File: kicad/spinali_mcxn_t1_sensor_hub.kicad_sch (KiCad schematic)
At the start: 0 parts

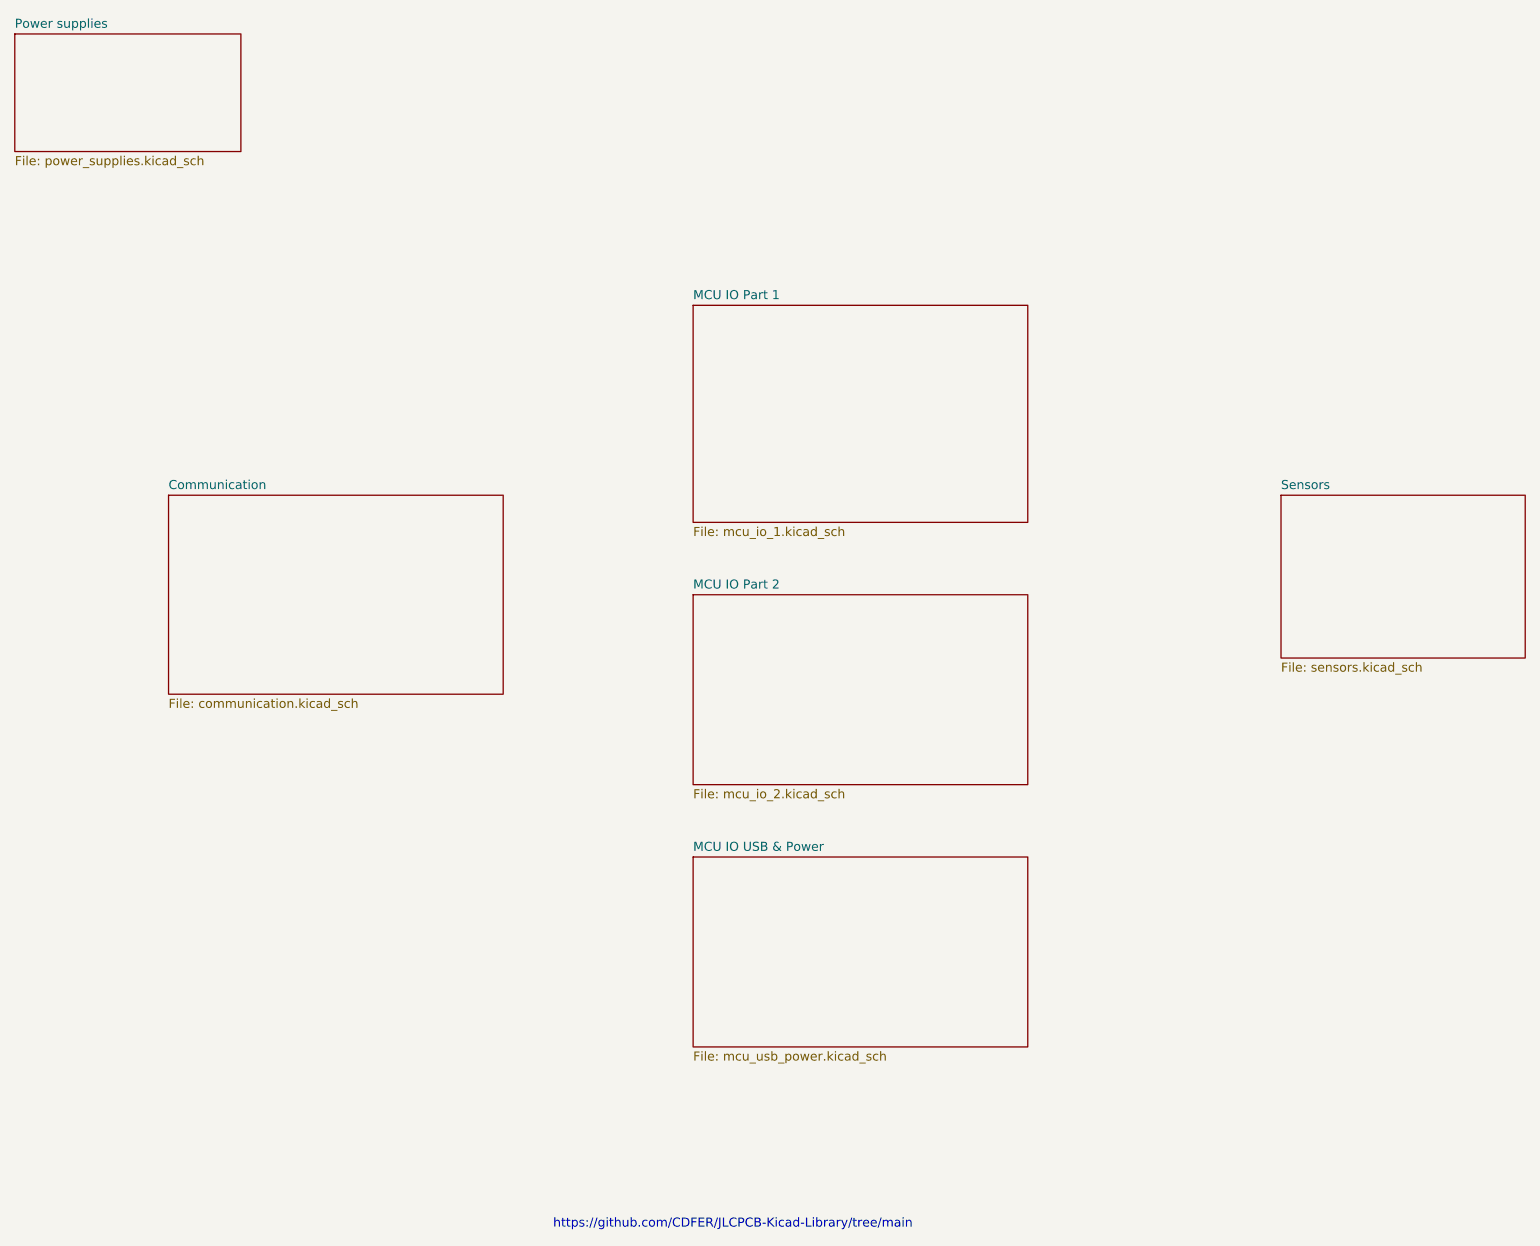
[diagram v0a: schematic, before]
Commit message: Updated schematics and BOM.
- Finished power supply schematics
- Added power schematic around MCXN
- Assigned MCXN pins
- Created board-to-board schematic and assigned pins to DF40T board-to-board connector
- Added correct sensors, finished sensor schematic
- Updated parts in communication schematic
- Added all part numbers etc in parts parameters
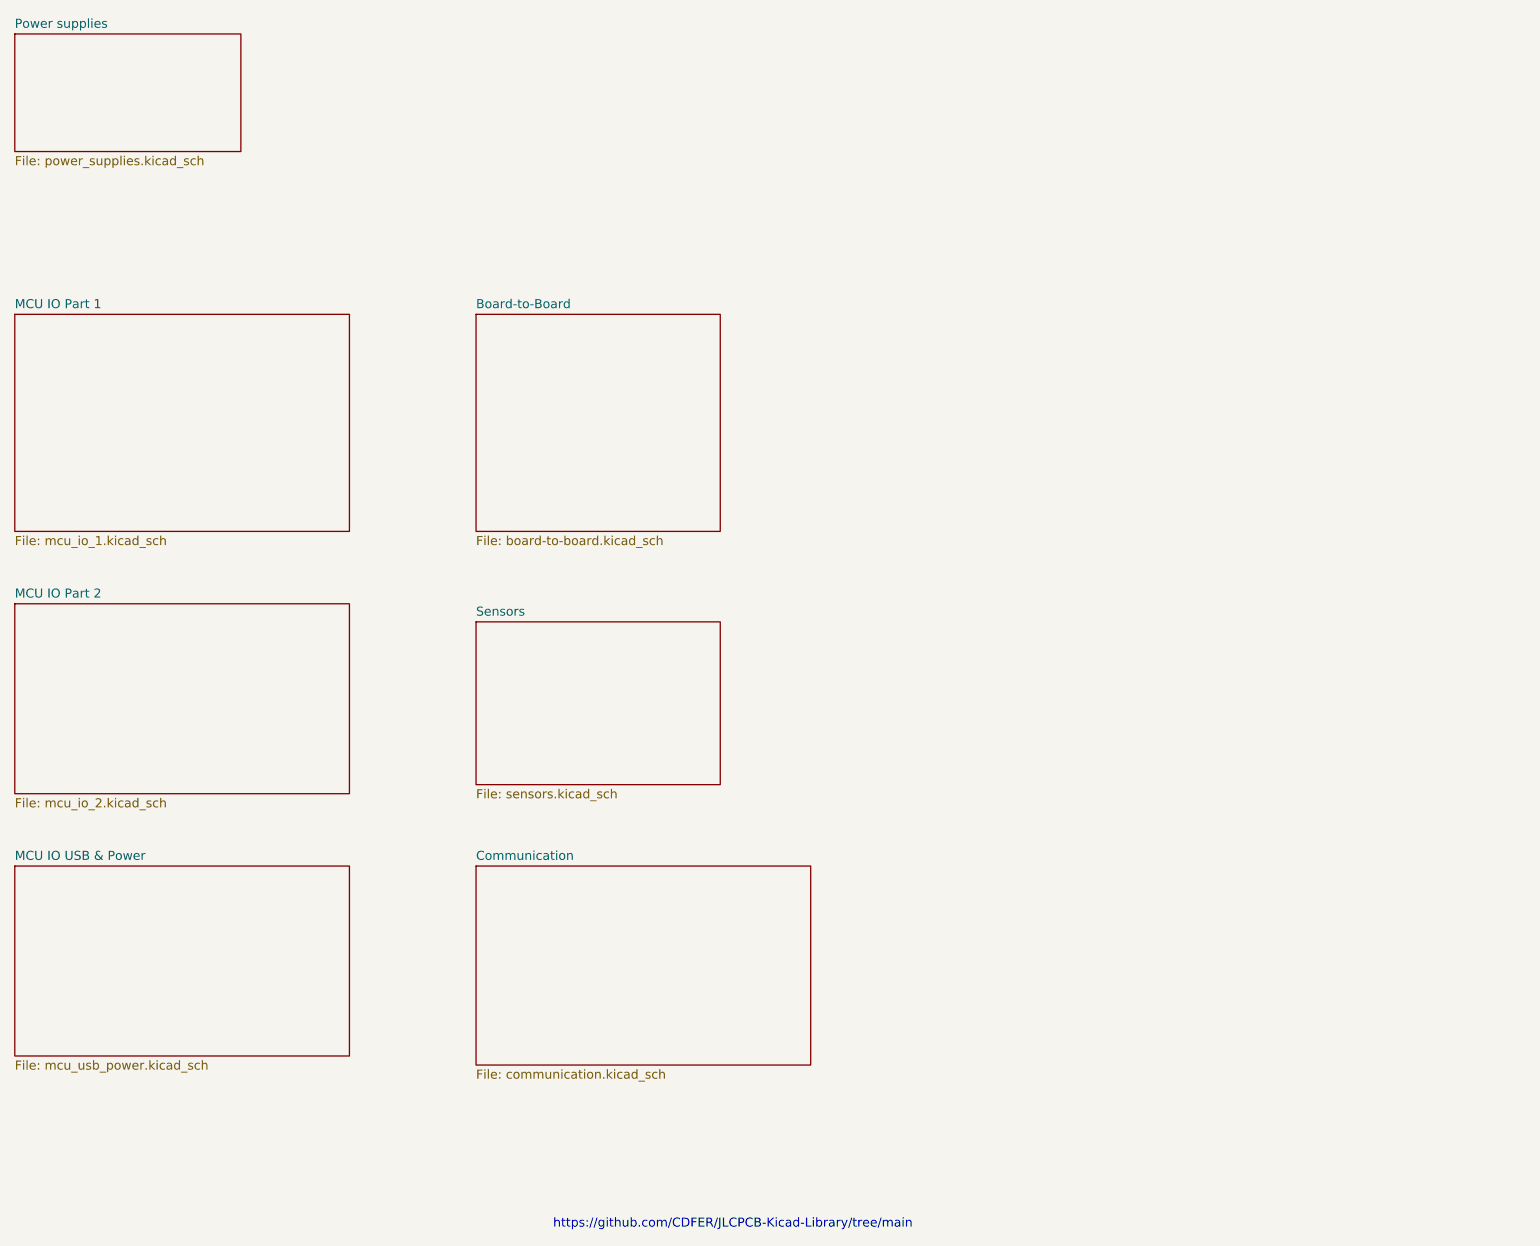
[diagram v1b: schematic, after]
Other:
- added sheet Board-to-Board (board-to-board.kicad_sch)
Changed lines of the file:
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@@
 	)
 	(sheet
-		(at 115.57 62.23)
+		(at 85.09 63.5)
+		(size 34.29 30.48)
+		(fields_autoplaced yes)
+		(stroke
+			(width 0.1524)
+			(type solid)
+		)
+		(fill
+			(color 0 0 0 0.0000)
+		)
+		(property "Sheetname" "Board-to-Board"
+			(at 85.09 62.7884 0)
+			(effects
+				(font
+					(size 1.27 1.27)
+				)
+				(justify left bottom)
+			)
+		)
+		(property "Sheetfile" "board-to-board.kicad_sch"
+			(at 85.09 94.5646 0)
+			(effects
+				(font
+					(size 1.27 1.27)
+				)
+				(justify left top)
+			)
+		)
+		(instances
+			(project "spinali_mcxn_t1_sensor_hub"
+				(path "/8b469ec1-e800-4d46-8a32-95d77ceae6db"
+					(page "8")
+				)
+			)
+		)
+	)
+	(sheet
+		(at 20.32 63.5)
 		(size 46.99 30.48)
 		(fields_autoplaced yes)
@@
 		)
 		(property "Sheetname" "MCU IO Part 1"
-			(at 115.57 61.5184 0)
+			(at 20.32 62.7884 0)
 			(effects
 				(font
@@
 		)
 		(property "Sheetfile" "mcu_io_1.kicad_sch"
-			(at 115.57 93.2946 0)
+			(at 20.32 94.5646 0)
 			(effects
 				(font
@@
 	)
 	(sheet
-		(at 115.57 102.87)
+		(at 20.32 104.14)
 		(size 46.99 26.67)
 		(fields_autoplaced yes)
@@
 		)
 		(property "Sheetname" "MCU IO Part 2"
-			(at 115.57 102.1584 0)
+			(at 20.32 103.4284 0)
 			(effects
 				(font
@@
 		)
 		(property "Sheetfile" "mcu_io_2.kicad_sch"
-			(at 115.57 130.1246 0)
+			(at 20.32 131.3946 0)
 			(effects
 				(font
@@
 	)
 	(sheet
-		(at 198.12 88.9)
+		(at 85.09 106.68)
 		(size 34.29 22.86)
 		(fields_autoplaced yes)
@@
 		)
 		(property "Sheetname" "Sensors"
-			(at 198.12 88.1884 0)
+			(at 85.09 105.9684 0)
 			(effects
 				(font
@@
 		)
 		(property "Sheetfile" "sensors.kicad_sch"
-			(at 198.12 112.3446 0)
+			(at 85.09 130.1246 0)
 			(effects
 				(font
@@
 	)
 	(sheet
-		(at 41.91 88.9)
+		(at 85.09 140.97)
 		(size 46.99 27.94)
 		(fields_autoplaced yes)
@@
 		)
 		(property "Sheetname" "Communication"
-			(at 41.91 88.1884 0)
+			(at 85.09 140.2584 0)
 			(effects
 				(font
@@
 		)
 		(property "Sheetfile" "communication.kicad_sch"
-			(at 41.91 117.4246 0)
+			(at 85.09 169.4946 0)
 			(effects
 				(font
@@
 	)
 	(sheet
-		(at 115.57 139.7)
+		(at 20.32 140.97)
 		(size 46.99 26.67)
 		(fields_autoplaced yes)
@@
 		)
 		(property "Sheetname" "MCU IO USB & Power"
-			(at 115.57 138.9884 0)
+			(at 20.32 140.2584 0)
 			(effects
 				(font
@@
 		)
 		(property "Sheetfile" "mcu_usb_power.kicad_sch"
-			(at 115.57 166.9546 0)
-			(effects
-				(font
+			(at 20.32 168.2246 0)
+			(effects
+				(font

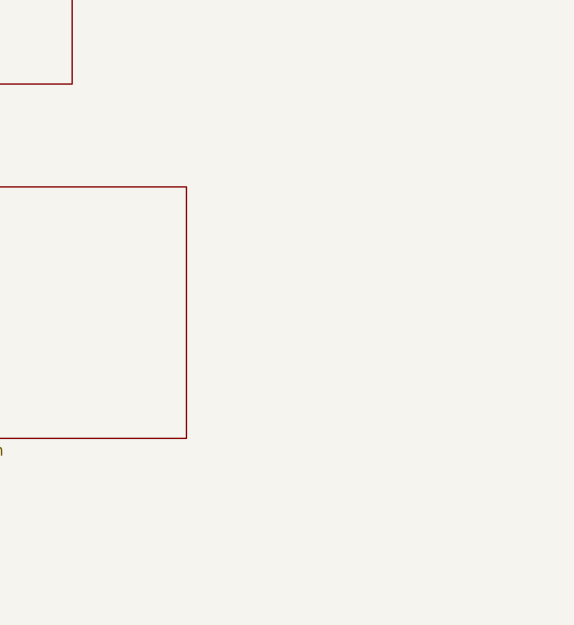
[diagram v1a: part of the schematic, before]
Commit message: Finished schematic design for first review
Finished schematic design for first review.
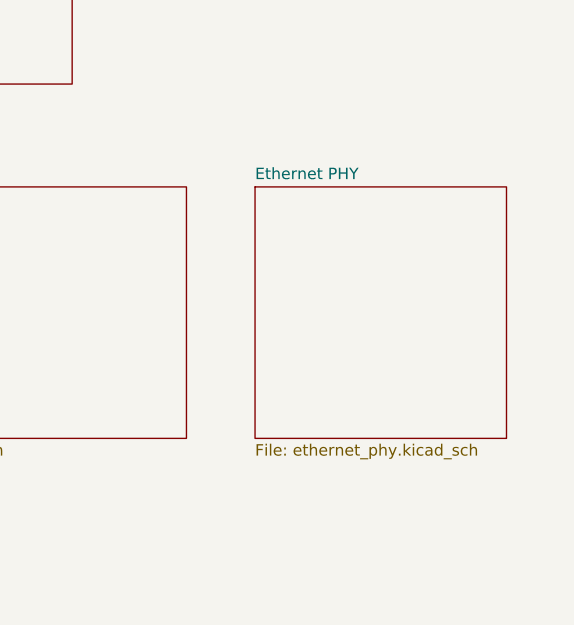
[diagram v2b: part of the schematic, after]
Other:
- added sheet Ethernet PHY (ethernet_phy.kicad_sch)
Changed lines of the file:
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@@
+	)
+	(sheet
+		(at 139.7 140.97)
+		(size 27.94 27.94)
+		(fields_autoplaced yes)
+		(stroke
+			(width 0.1524)
+			(type solid)
+		)
+		(fill
+			(color 0 0 0 0.0000)
+		)
+		(property "Sheetname" "Ethernet PHY"
+			(at 139.7 140.2584 0)
+			(effects
+				(font
+					(size 1.27 1.27)
+				)
+				(justify left bottom)
+			)
+		)
+		(property "Sheetfile" "ethernet_phy.kicad_sch"
+			(at 139.7 169.4946 0)
+			(effects
+				(font
+					(size 1.27 1.27)
+				)
+				(justify left top)
+			)
+		)
+		(instances
+			(project "spinali_mcxn_t1_sensor_hub"
+				(path "/8b469ec1-e800-4d46-8a32-95d77ceae6db"
+					(page "9")
+				)
+			)
+		)
 	)
 	(sheet
